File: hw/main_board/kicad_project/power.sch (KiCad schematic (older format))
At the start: 0 parts

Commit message: starting power supply design, still collecting notes
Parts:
- added BT? (x2): 9V, symbol BATTERY
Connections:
- net AGND: now also BT?.1 (+), BT?.2 (-)
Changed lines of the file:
@@
 $Descr A4 11693 8268
 encoding utf-8
-Sheet 3 7
+Sheet 2 7
 Title ""
 Date "26 feb 2014"
@@
 Comment4 ""
 $EndDescr
-Text HLabel 4850 5700 0    60   Input ~ 0
+Text HLabel 1550 5300 0    60   Input ~ 0
 DGND
-Text HLabel 5100 3450 0    60   Input ~ 0
+Text HLabel 1800 3050 0    60   Input ~ 0
 D3V3
-Text HLabel 5100 4550 0    60   Input ~ 0
+Text HLabel 1800 4150 0    60   Input ~ 0
 MUXVSS
-Text HLabel 5050 4300 0    60   Input ~ 0
+Text HLabel 1750 3900 0    60   Input ~ 0
 MUXVDD
 Text HLabel 10100 5600 2    60   Input ~ 0
@@
 Text HLabel 10050 3700 2    60   Input ~ 0
 A3V3
+$Comp
+L BATTERY BT?
+U 1 1 53166C7A
+P 3650 3250
+F 0 "BT?" H 3650 3450 50  0000 C CNN
+F 1 "9V" H 3650 3060 50  0000 C CNN
+F 2 "" H 3650 3250 60  0000 C CNN
+F 3 "" H 3650 3250 60  0000 C CNN
+	1    3650 3250
+	0    1    1    0
+$EndComp
+$Comp
+L BATTERY BT?
+U 1 1 53166C87
+P 3650 4050
+F 0 "BT?" H 3650 4250 50  0000 C CNN
+F 1 "9V" H 3650 3860 50  0000 C CNN
+F 2 "" H 3650 4050 60  0000 C CNN
+F 3 "" H 3650 4050 60  0000 C CNN
+	1    3650 4050
+	0    1    1    0
+$EndComp
+$Comp
+L AGND #PWR?
+U 1 1 53166C99
+P 3500 3650
+F 0 "#PWR?" H 3500 3650 40  0001 C CNN
+F 1 "AGND" H 3500 3580 50  0000 C CNN
+F 2 "" H 3500 3650 60  0000 C CNN
+F 3 "" H 3500 3650 60  0000 C CNN
+	1    3500 3650
+	0    1    1    0
+$EndComp
+$Comp
+L DGND #PWR?
+U 1 1 53166CC2
+P 3800 3650
+F 0 "#PWR?" H 3800 3650 40  0001 C CNN
+F 1 "DGND" H 3800 3580 40  0000 C CNN
+F 2 "" H 3800 3650 60  0000 C CNN
+F 3 "" H 3800 3650 60  0000 C CNN
+	1    3800 3650
+	0    -1   -1   0
+$EndComp
+Wire Wire Line
+	3650 3750 3650 3550
+Wire Wire Line
+	3800 3650 3500 3650
+Connection ~ 3650 3650
 $EndSCHEMATC

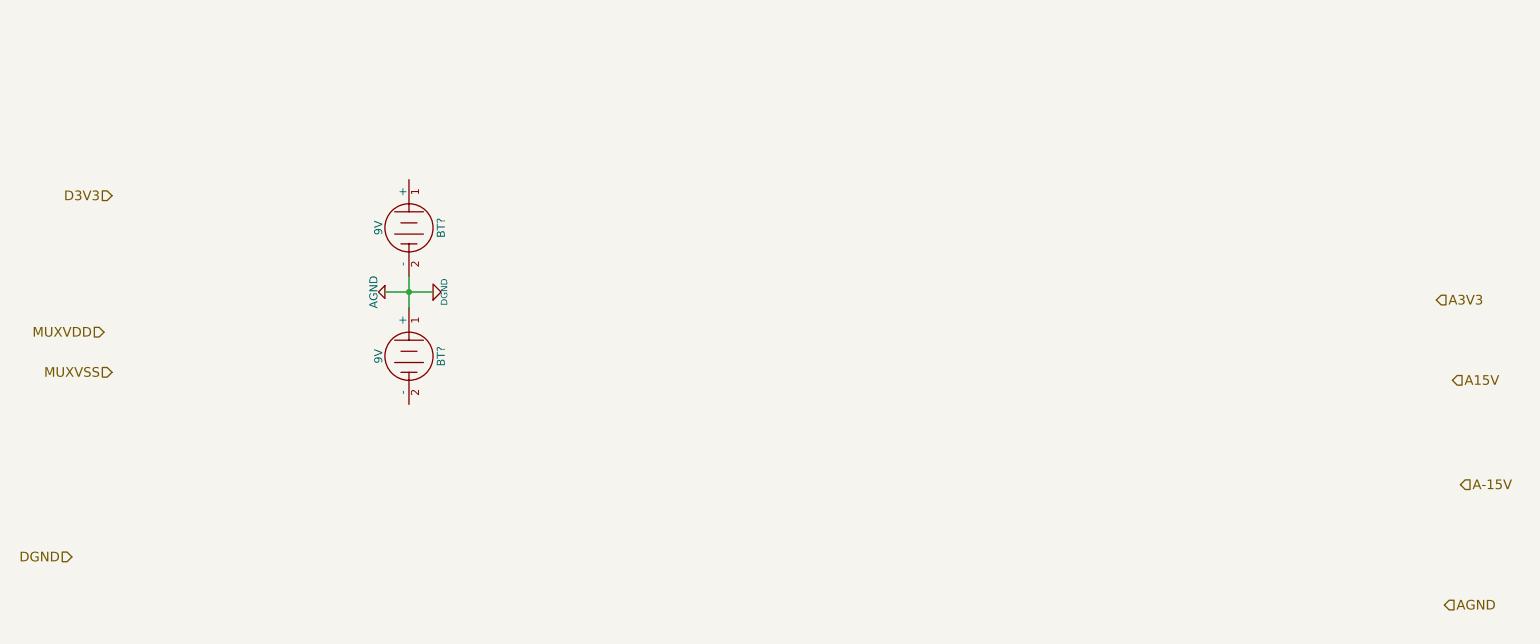
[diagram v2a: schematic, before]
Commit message: started mainboard pcb layout, fixing small things in schematic, TODO: schematic connector symbols and pads
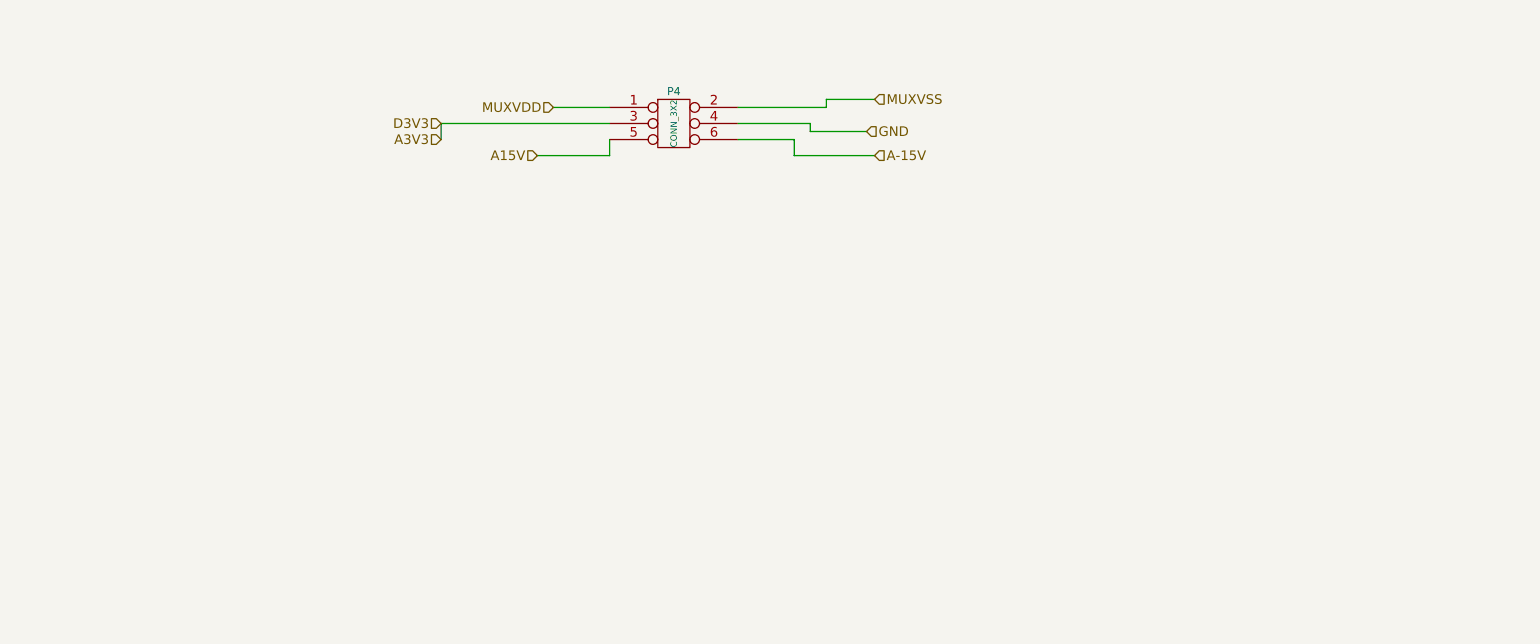
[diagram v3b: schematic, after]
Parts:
- removed BT? (x2): 9V, symbol BATTERY
- added P4: CONN_3X2, symbol CONN_3X2
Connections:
- net A-15V: now also P4.6
- net A15V: now also P4.5
- net A3V3: now also P4.3
- net MUXVDD: now also P4.1
- net MUXVSS: now also P4.2
- new net GND: P4.4
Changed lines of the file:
@@
 Sheet 2 7
 Title ""
-Date "26 feb 2014"
-Rev ""
+Date "01 Feb 2014"
+Rev "A"
 Comp ""
-Comment1 ""
+Comment1 "Copyright 2014 Andrey Shmakov"
 Comment2 ""
 Comment3 ""
 Comment4 ""
 $EndDescr
-Text HLabel 1550 5300 0    60   Input ~ 0
-DGND
-Text HLabel 1800 3050 0    60   Input ~ 0
+Text HLabel 3850 2600 0    60   Input ~ 0
 D3V3
-Text HLabel 1800 4150 0    60   Input ~ 0
+Text HLabel 6550 2450 2    60   Input ~ 0
 MUXVSS
-Text HLabel 1750 3900 0    60   Input ~ 0
+Text HLabel 4550 2500 0    60   Input ~ 0
 MUXVDD
-Text HLabel 10100 5600 2    60   Input ~ 0
-AGND
-Text HLabel 10200 4850 2    60   Input ~ 0
+Text HLabel 6500 2650 2    60   Input ~ 0
+GND
+Text HLabel 6550 2800 2    60   Input ~ 0
 A-15V
-Text HLabel 10150 4200 2    60   Input ~ 0
+Text HLabel 4450 2800 0    60   Input ~ 0
 A15V
-Text HLabel 10050 3700 2    60   Input ~ 0
+Text HLabel 3850 2700 0    60   Input ~ 0
 A3V3
 $Comp
-L BATTERY BT?
-U 1 1 53166C7A
-P 3650 3250
-F 0 "BT?" H 3650 3450 50  0000 C CNN
-F 1 "9V" H 3650 3060 50  0000 C CNN
-F 2 "" H 3650 3250 60  0000 C CNN
-F 3 "" H 3650 3250 60  0000 C CNN
-	1    3650 3250
-	0    1    1    0
-$EndComp
-$Comp
-L BATTERY BT?
-U 1 1 53166C87
-P 3650 4050
-F 0 "BT?" H 3650 4250 50  0000 C CNN
-F 1 "9V" H 3650 3860 50  0000 C CNN
-F 2 "" H 3650 4050 60  0000 C CNN
-F 3 "" H 3650 4050 60  0000 C CNN
-	1    3650 4050
-	0    1    1    0
-$EndComp
-$Comp
-L AGND #PWR?
-U 1 1 53166C99
-P 3500 3650
-F 0 "#PWR?" H 3500 3650 40  0001 C CNN
-F 1 "AGND" H 3500 3580 50  0000 C CNN
-F 2 "" H 3500 3650 60  0000 C CNN
-F 3 "" H 3500 3650 60  0000 C CNN
-	1    3500 3650
-	0    1    1    0
-$EndComp
-$Comp
-L DGND #PWR?
-U 1 1 53166CC2
-P 3800 3650
-F 0 "#PWR?" H 3800 3650 40  0001 C CNN
-F 1 "DGND" H 3800 3580 40  0000 C CNN
-F 2 "" H 3800 3650 60  0000 C CNN
-F 3 "" H 3800 3650 60  0000 C CNN
-	1    3800 3650
-	0    -1   -1   0
+L CONN_3X2 P4
+U 1 1 53181BA1
+P 5300 2650
+F 0 "P4" H 5300 2900 50  0000 C CNN
+F 1 "CONN_3X2" V 5300 2700 40  0000 C CNN
+F 2 "" H 5300 2650 60  0000 C CNN
+F 3 "" H 5300 2650 60  0000 C CNN
+	1    5300 2650
+	1    0    0    -1
 $EndComp
 Wire Wire Line
-	3650 3750 3650 3550
+	5700 2500 6250 2500
 Wire Wire Line
-	3800 3650 3500 3650
-Connection ~ 3650 3650
+	6250 2500 6250 2450
+Wire Wire Line
+	6250 2450 6550 2450
+Wire Wire Line
+	6500 2650 6150 2650
+Wire Wire Line
+	6150 2650 6150 2600
+Wire Wire Line
+	6150 2600 5700 2600
+Wire Wire Line
+	5700 2700 6050 2700
+Wire Wire Line
+	6050 2700 6050 2800
+Wire Wire Line
+	6050 2800 6550 2800
+Wire Wire Line
+	4900 2500 4550 2500
+Wire Wire Line
+	4900 2600 3850 2600
+Wire Wire Line
+	3850 2600 3850 2700
+Wire Wire Line
+	4450 2800 4900 2800
+Wire Wire Line
+	4900 2800 4900 2700
 $EndSCHEMATC

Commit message: final rework of mux board, finalizing stacking connectors, almost there
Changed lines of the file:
@@
 EESchema Schematic File Version 2
-LIBS:power
-LIBS:device
-LIBS:transistors
-LIBS:conn
-LIBS:linear
-LIBS:regul
-LIBS:74xx
-LIBS:cmos4000
-LIBS:adc-dac
-LIBS:memory
-LIBS:xilinx
-LIBS:special
-LIBS:microcontrollers
-LIBS:dsp
-LIBS:microchip
-LIBS:analog_switches
-LIBS:motorola
-LIBS:texas
-LIBS:intel
-LIBS:audio
-LIBS:interface
-LIBS:digital-audio
-LIBS:philips
-LIBS:display
-LIBS:cypress
-LIBS:siliconi
-LIBS:opto
-LIBS:atmel
-LIBS:contrib
-LIBS:valves
 LIBS:ddslib
-LIBS:demuxcomplib
-LIBS:tdsc-kicad-convert
 LIBS:tDCS_driver-cache
 EELAYER 24 0
@@
 Wire Wire Line
 	4900 2800 4900 2700
+$Comp
+L PWR_FLAG #FLG08
+U 1 1 531D1B0E
+P 5700 2500
+F 0 "#FLG08" H 5700 2595 30  0001 C CNN
+F 1 "PWR_FLAG" H 5700 2680 30  0000 C CNN
+F 2 "" H 5700 2500 60  0000 C CNN
+F 3 "" H 5700 2500 60  0000 C CNN
+	1    5700 2500
+	1    0    0    -1
+$EndComp
+$Comp
+L PWR_FLAG #FLG09
+U 1 1 531D1B1B
+P 6450 2650
+F 0 "#FLG09" H 6450 2745 30  0001 C CNN
+F 1 "PWR_FLAG" H 6450 2830 30  0000 C CNN
+F 2 "" H 6450 2650 60  0000 C CNN
+F 3 "" H 6450 2650 60  0000 C CNN
+	1    6450 2650
+	1    0    0    -1
+$EndComp
+$Comp
+L PWR_FLAG #FLG010
+U 1 1 531D1B21
+P 6400 2800
+F 0 "#FLG010" H 6400 2895 30  0001 C CNN
+F 1 "PWR_FLAG" H 6400 2980 30  0000 C CNN
+F 2 "" H 6400 2800 60  0000 C CNN
+F 3 "" H 6400 2800 60  0000 C CNN
+	1    6400 2800
+	1    0    0    -1
+$EndComp
+$Comp
+L PWR_FLAG #FLG011
+U 1 1 531D1B27
+P 4900 2500
+F 0 "#FLG011" H 4900 2595 30  0001 C CNN
+F 1 "PWR_FLAG" H 4900 2680 30  0000 C CNN
+F 2 "" H 4900 2500 60  0000 C CNN
+F 3 "" H 4900 2500 60  0000 C CNN
+	1    4900 2500
+	1    0    0    -1
+$EndComp
+$Comp
+L PWR_FLAG #FLG012
+U 1 1 531D1B2D
+P 3950 2600
+F 0 "#FLG012" H 3950 2695 30  0001 C CNN
+F 1 "PWR_FLAG" H 3950 2780 30  0000 C CNN
+F 2 "" H 3950 2600 60  0000 C CNN
+F 3 "" H 3950 2600 60  0000 C CNN
+	1    3950 2600
+	1    0    0    -1
+$EndComp
+$Comp
+L PWR_FLAG #FLG013
+U 1 1 531D1B33
+P 4850 2800
+F 0 "#FLG013" H 4850 2895 30  0001 C CNN
+F 1 "PWR_FLAG" H 4850 2980 30  0000 C CNN
+F 2 "" H 4850 2800 60  0000 C CNN
+F 3 "" H 4850 2800 60  0000 C CNN
+	1    4850 2800
+	1    0    0    -1
+$EndComp
+Connection ~ 6450 2650
+Connection ~ 6400 2800
+Connection ~ 4850 2800
+Connection ~ 3950 2600
 $EndSCHEMATC
